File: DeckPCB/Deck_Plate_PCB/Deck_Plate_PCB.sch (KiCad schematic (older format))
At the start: 69 parts, among them J1 Raspberry_Pi_2_3, J2 NASA_Telemetry_Interface, J3 NASA PWR_Interface, J4 Motor_Inhibit, J5 SunnyBuddy_Inhibit, J6 Batt_JST_Conn, J7 BurWire_Inhibit, P1 Digital, P10 CONN_01X01, P11 CONN_01X01, P12 CONN_01X01, P13 CONN_01X01, P2 Power, P3 Analog, P4 Analog, P5 PWM, P6 PWM, P7 Communication, P8 CONN_01X01, P9 CONN_01X01, Q1 Q_NPN_BCE, Q2 2N7000, Q3 2N7000, U1 Adafruit_INA219_Breakout, U10 LM20, U11 Big_Easy_Driver, U12 Pi_Cam, U13 LM20, U2 LM2576T-5, U3 D24V25F9, U4 SunnyBuddy_Breakout, U5 LM2576T-5, U6 SF_Logic_Level_Conv, U7 Lidar_RangeFinder, U8 ADXL377, U9 TTL_Camera

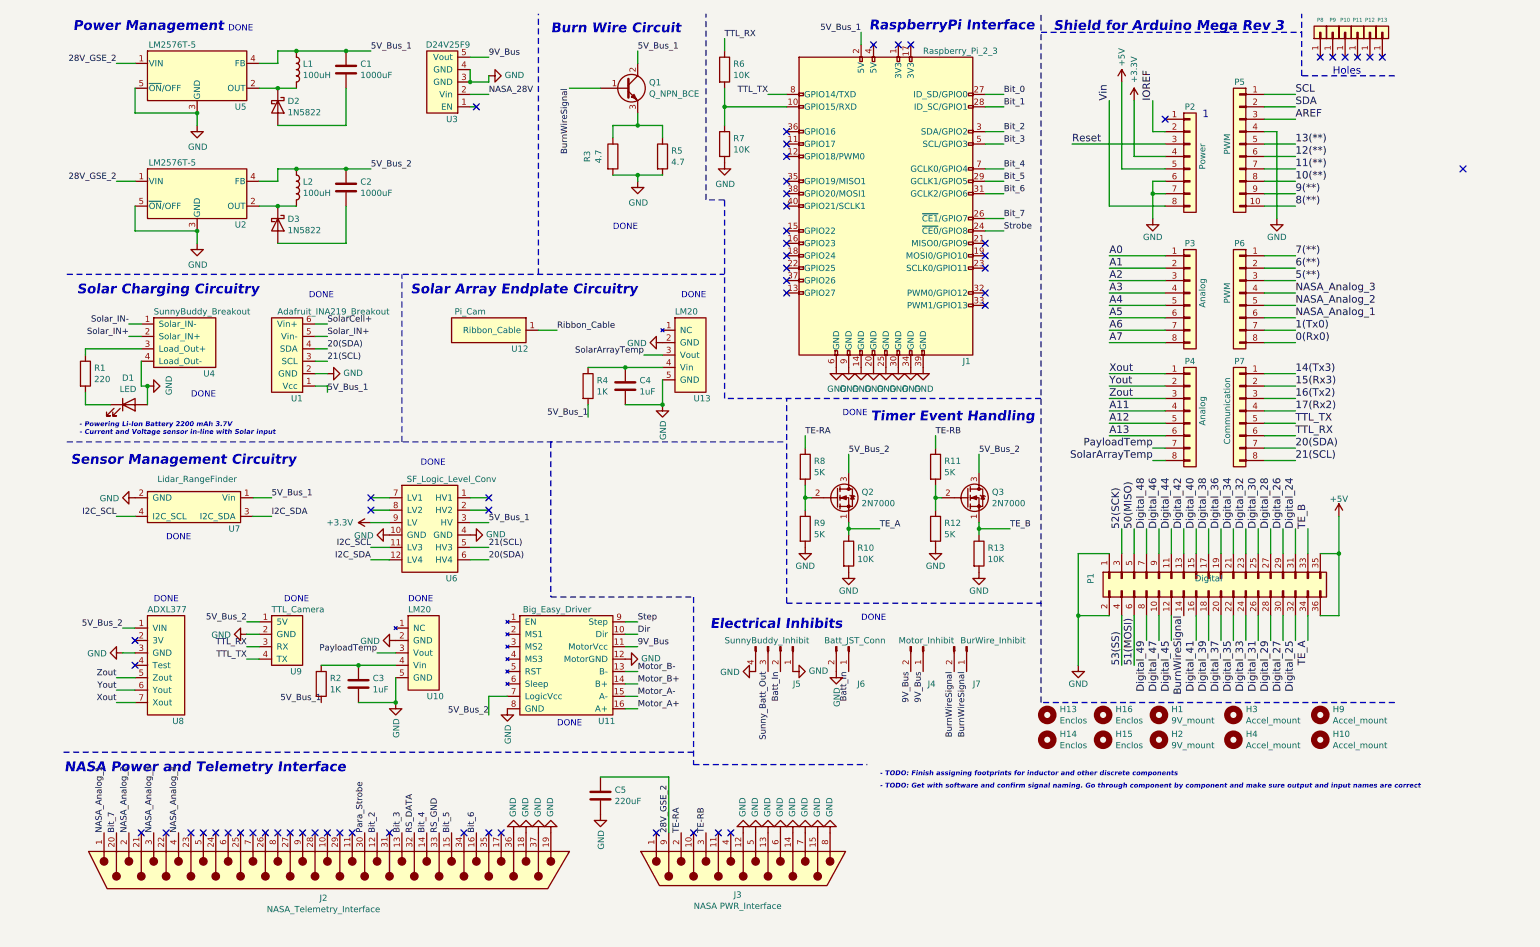
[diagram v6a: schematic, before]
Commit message: Created new daughter board for SunnyBuddy and RaspPi. Initial component layout complete.
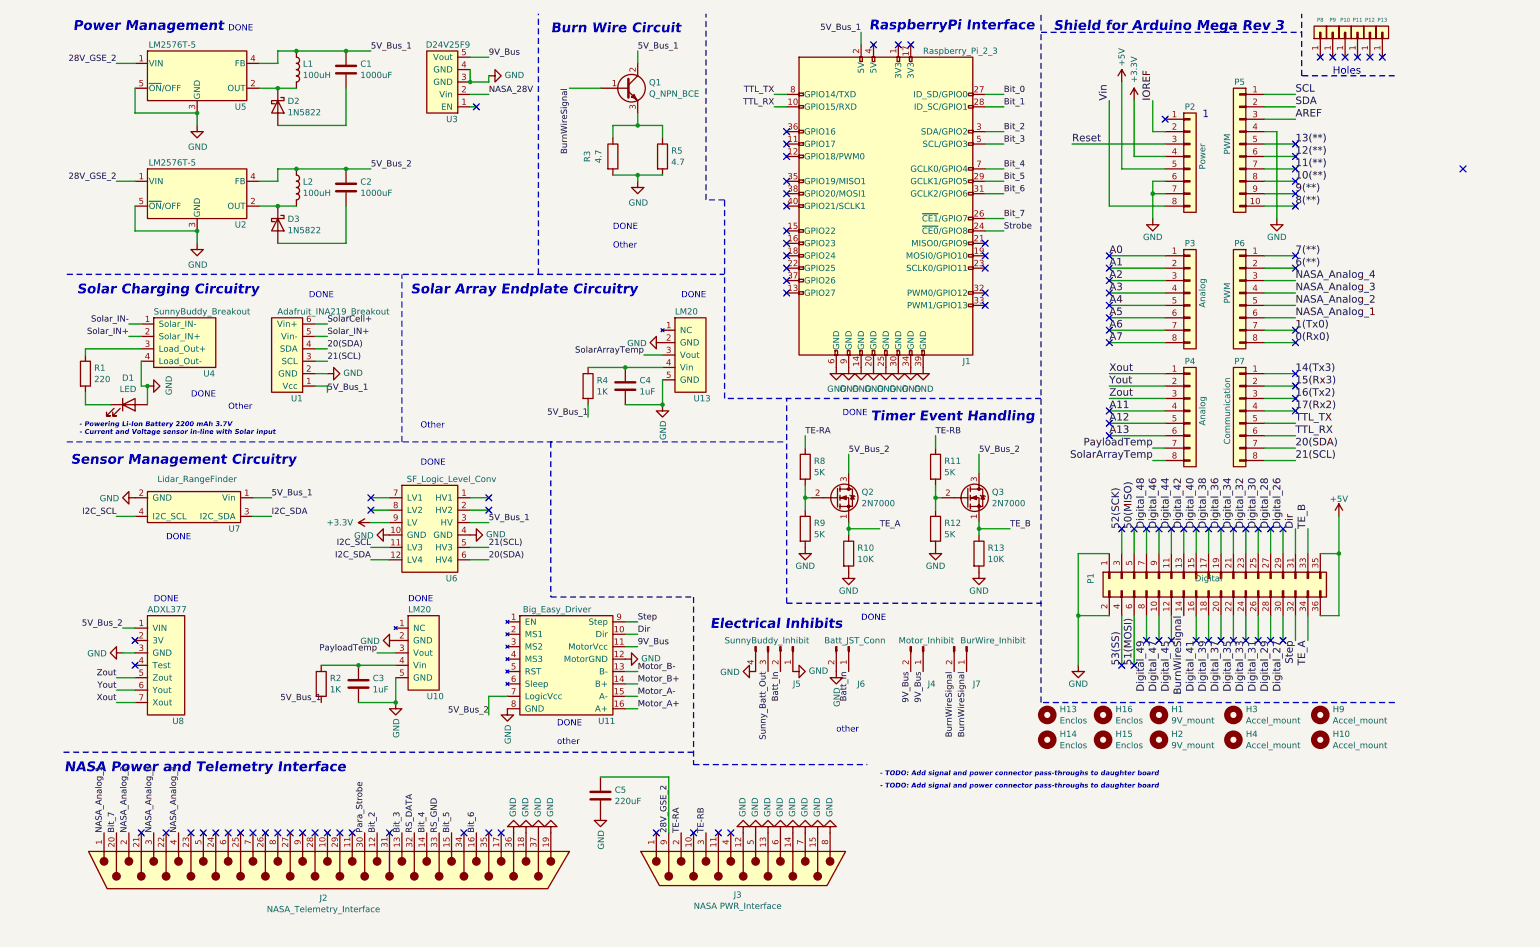
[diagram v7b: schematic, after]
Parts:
- removed R6, R7: 10K, Resistor_THT:R_Axial_DIN0207_L6.3mm_D2.5mm_P10.16mm_Horizontal, symbol Device:R
- removed U12: Pi_Cam, symbol Deck_Plate_PCB:Pi_Cam
- removed U9: TTL_Camera, Connector_PinHeader_2.54mm:PinHeader_1x04_P2.54mm_Vertical, symbol Deck_Plate_PCB:TTL_Camera
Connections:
- net 5(**) is gone; now on net NASA_Analog_4: P6.3 (Pin_3)
- net Digital_24 is gone; now on net Dir: P1.31 (Pin_31)
- net Digital_25 is gone; now on net Step: P1.32 (Pin_32)
- net TTL_RX: now also J1.10 (GPIO15/RXD)
- no-connect marks 59 -> 111
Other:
- note added: "- TODO: Add signal and power connector pass-throughs to daughter board\n"
- note added: "Other"
- note added: "Other\n"
- note added: "other"
- note added: "other\n"
- note removed: "- TODO: Finish assigning footprints for inductor and other discrete components\n"
- note removed: "- TODO: Get with software and confirm signal naming. Go through component by component and make sure output and input names are correct"
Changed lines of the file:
@@
 TE_B
 Text Label 10400 4650 1    60   ~ 0
-Digital_24
+Dir
 Text Label 10300 4650 1    60   ~ 0
 Digital_26
@@
 TE_A
 Text Label 10400 5550 3    60   ~ 0
-Digital_25
+Step
 Text Label 10300 5550 3    60   ~ 0
 Digital_27
@@
 6(**)
 Text Label 10400 2650 0    60   ~ 0
-5(**)
+NASA_Analog_4
 Text Label 10400 2750 0    60   ~ 0
 NASA_Analog_3
@@
 $EndComp
 $Comp
-L power:GND #PWR0114
-U 1 1 5E59C862
-P 5800 1700
-F 0 "#PWR0114" H 5800 1450 50  0001 C CNN
-F 1 "GND" H 5805 1527 50  0000 C CNN
-F 2 "" H 5800 1700 50  0001 C CNN
-F 3 "" H 5800 1700 50  0001 C CNN
-	1    5800 1700
-	1    0    0    -1
-$EndComp
-Text Label 5800 700  0    50   ~ 0
-TTL_RX
-Wire Wire Line
-	5800 800  5800 700
-$Comp
-L Device:R R6
-U 1 1 5E590153
-P 5800 950
-F 0 "R6" H 5870 996 50  0000 L CNN
-F 1 "10K" H 5870 905 50  0000 L CNN
-F 2 "Resistor_THT:R_Axial_DIN0207_L6.3mm_D2.5mm_P10.16mm_Horizontal" V 5730 950 50  0001 C CNN
-F 3 "~" H 5800 950 50  0001 C CNN
-	1    5800 950
-	1    0    0    -1
-$EndComp
-$Comp
-L Device:R R7
-U 1 1 5E58F78F
-P 5800 1550
-F 0 "R7" H 5870 1596 50  0000 L CNN
-F 1 "10K" H 5870 1505 50  0000 L CNN
-F 2 "Resistor_THT:R_Axial_DIN0207_L6.3mm_D2.5mm_P10.16mm_Horizontal" V 5730 1550 50  0001 C CNN
-F 3 "~" H 5800 1550 50  0001 C CNN
-	1    5800 1550
-	1    0    0    -1
-$EndComp
-Wire Wire Line
-	5800 1250 5800 1400
-Connection ~ 5800 1250
-Wire Wire Line
-	5800 1100 5800 1250
-Wire Wire Line
-	6300 1250 5800 1250
-Text Label 6150 1150 2    50   ~ 0
-TTL_TX
-Wire Wire Line
-	6300 1150 6150 1150
-$Comp
 L power:GND #PWR0115
 U 1 1 5E56BFDB
@@
 Wire Notes Line
 	500  2600 5800 2600
-$Comp
-L Deck_Plate_PCB:TTL_Camera U9
-U 1 1 5E7B135A
-P 1600 5900
-F 0 "U9" H 2300 6000 50  0000 L CNN
-F 1 "TTL_Camera" H 2150 6500 50  0000 L CNN
-F 2 "Connector_PinHeader_2.54mm:PinHeader_1x04_P2.54mm_Vertical" H 1600 5900 50  0001 C CNN
-F 3 "https://learn.adafruit.com/ttl-serial-camera" H 1600 5900 50  0001 C CNN
-	1    1600 5900
-	1    0    0    -1
-$EndComp
-Wire Wire Line
-	2050 5400 1950 5400
-Wire Wire Line
-	2050 5500 1950 5500
-Wire Wire Line
-	2050 5600 1950 5600
-Wire Wire Line
-	2050 5700 1950 5700
-Text Label 1950 5400 2    50   ~ 0
-5V_Bus_2
-$Comp
-L power:GND #PWR0124
-U 1 1 5E80010A
-P 1950 5500
-F 0 "#PWR0124" H 1950 5250 50  0001 C CNN
-F 1 "GND" V 1955 5372 50  0000 R CNN
-F 2 "" H 1950 5500 50  0001 C CNN
-F 3 "" H 1950 5500 50  0001 C CNN
-	1    1950 5500
-	0    1    1    0
-$EndComp
-Text Label 1950 5600 2    50   ~ 0
-TTL_RX
-Text Label 1950 5700 2    50   ~ 0
-TTL_TX
 $Comp
 L Deck_Plate_PCB:LM20 U10
@@
 	0    1    1    0
 $EndComp
-$Comp
-L Deck_Plate_PCB:Pi_Cam U12
-U 1 1 5E9ED3E3
-P 3500 3450
-F 0 "U12" H 4150 3700 50  0000 C CNN
-F 1 "Pi_Cam" H 3750 4000 50  0000 C CNN
-F 2 "" H 3500 3450 50  0001 C CNN
-F 3 "" H 3500 3450 50  0001 C CNN
-	1    3500 3450
-	1    0    0    -1
-$EndComp
-Wire Wire Line
-	4300 3050 4450 3050
-Text Label 4450 3050 0    50   ~ 0
-Ribbon_Cable
 Text Notes 2050 2900 2    79   Italic 16
 Solar Charging Circuitry\n\n
-Text Notes 5100 2900 2    79   Italic 16
-Solar Array Endplate Circuitry\n\n
 Wire Notes Line
 	500  3950 6300 3950
@@
 $EndComp
 Text Notes 7050 6650 0    39   Italic 8
-- TODO: Finish assigning footprints for inductor and other discrete components\n
-Text Notes 7050 6750 0    39   Italic 8
-- TODO: Get with software and confirm signal naming. Go through component by component and make sure output and input names are correct
+- TODO: Add signal and power connector pass-throughs to daughter board\n
 $Comp
 L Connector:Conn_01x02_Male J4
@@
 DONE
 Text Notes 2450 2800 0    50   ~ 0
-DONE
-Text Notes 2250 5250 0    50   ~ 0
 DONE
 Text Notes 1200 5250 0    50   ~ 0
@@
 Text Label 2600 3100 0    50   ~ 0
 Solar_IN+
+Text Notes 3350 3850 0    50   ~ 0
+Other\n
+Text Notes 4450 6400 0    50   ~ 0
+other
+Text Notes 6700 6300 0    50   ~ 0
+other\n
+Text Notes 1800 3700 0    50   ~ 0
+Other\n
+Text Notes 4900 2400 0    50   ~ 0
+Other
+NoConn ~ 9200 4650
+NoConn ~ 9300 4650
+NoConn ~ 9400 4650
+NoConn ~ 9500 4650
+NoConn ~ 9600 4650
+NoConn ~ 9700 4650
+NoConn ~ 9800 4650
+NoConn ~ 9900 4650
+NoConn ~ 10000 4650
+NoConn ~ 10100 4650
+NoConn ~ 10200 4650
+NoConn ~ 10300 4650
+NoConn ~ 10300 5550
+NoConn ~ 10200 5550
+NoConn ~ 10100 5550
+NoConn ~ 10000 5550
+NoConn ~ 9900 5550
+NoConn ~ 9800 5550
+NoConn ~ 9700 5550
+NoConn ~ 9600 5550
+NoConn ~ 9400 5550
+NoConn ~ 9300 5550
+NoConn ~ 9200 5550
+NoConn ~ 9100 5750
+NoConn ~ 9000 5750
+NoConn ~ 9100 4650
+NoConn ~ 9000 4650
+NoConn ~ 8900 3700
+NoConn ~ 8900 3800
+NoConn ~ 8900 3900
+NoConn ~ 8900 3150
+NoConn ~ 8900 3050
+NoConn ~ 8900 2950
+NoConn ~ 8900 2850
+NoConn ~ 8900 2750
+NoConn ~ 8900 2650
+NoConn ~ 8900 2550
+NoConn ~ 8900 2450
+NoConn ~ 10400 2450
+NoConn ~ 10400 2550
+NoConn ~ 10400 3050
+NoConn ~ 10400 3150
+NoConn ~ 10400 1550
+NoConn ~ 10400 1650
+NoConn ~ 10400 1750
+NoConn ~ 10400 1850
+NoConn ~ 10400 1950
+NoConn ~ 10400 2050
+NoConn ~ 10400 3400
+NoConn ~ 10400 3500
+NoConn ~ 10400 3600
+NoConn ~ 10400 3700
+Wire Wire Line
+	6300 1150 6200 1150
+Wire Wire Line
+	6300 1250 6200 1250
+Text Label 6200 1150 2    50   ~ 0
+TTL_TX
+Text Label 6200 1250 2    50   ~ 0
+TTL_RX
+Text Notes 5100 2900 2    79   Italic 16
+Solar Array Endplate Circuitry\n\n
+Text Notes 7050 6750 0    39   Italic 8
+- TODO: Add signal and power connector pass-throughs to daughter board\n
 $EndSCHEMATC

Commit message: Started routing of Deck_Plate_PCB, the main board.
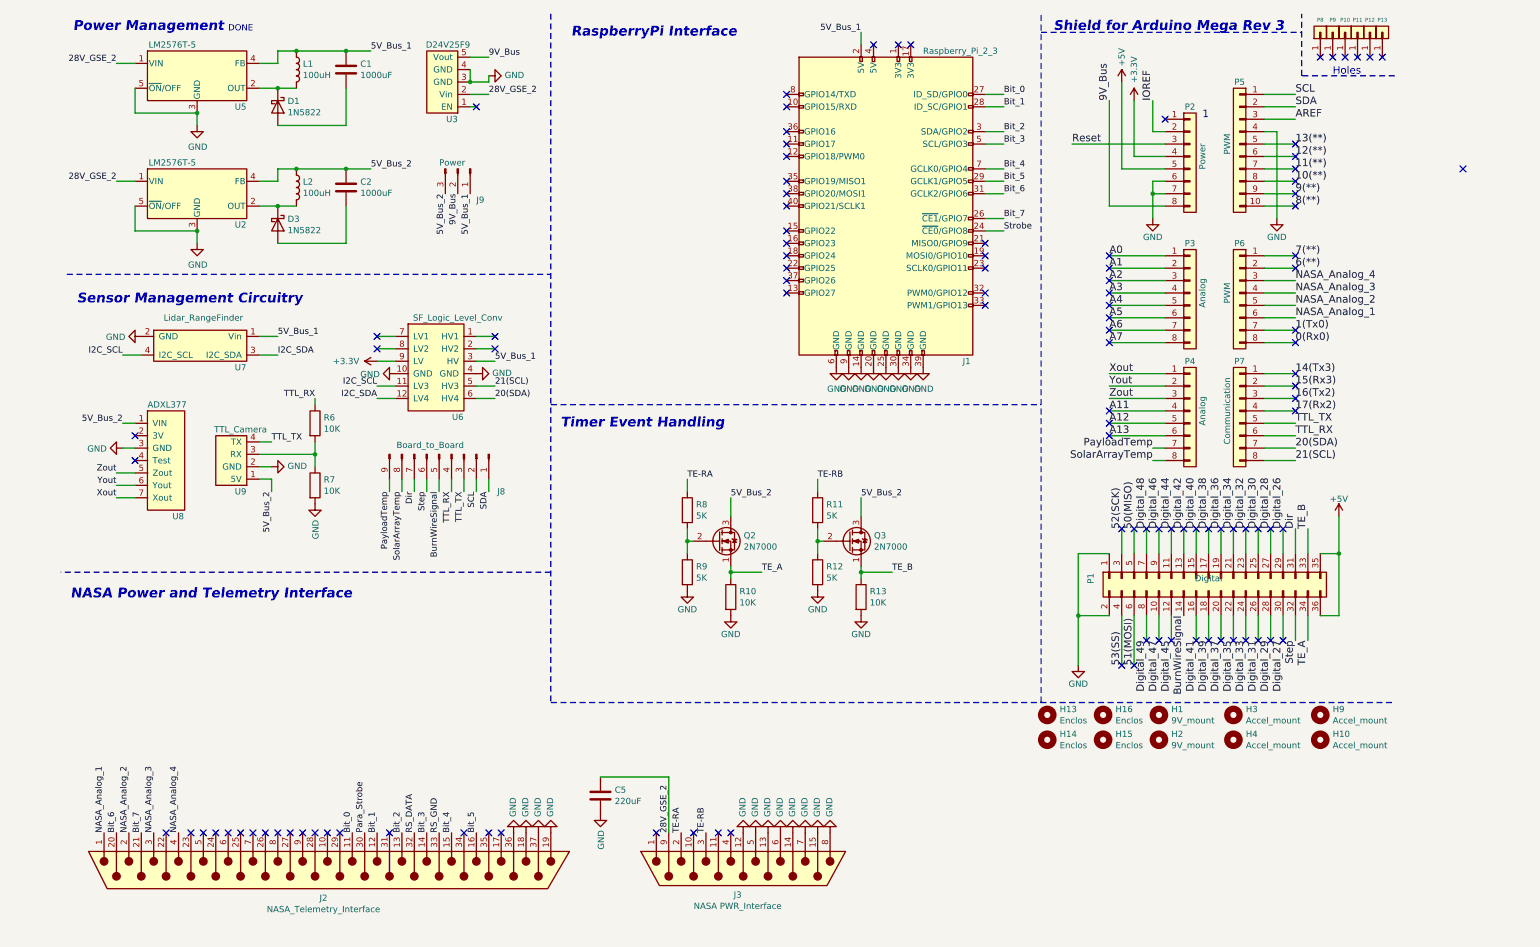
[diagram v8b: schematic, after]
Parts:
- removed C3, C4: 1uF, Capacitor_SMD:C_1206_3216Metric_Pad1.42x1.75mm_HandSolder, symbol Device:C
- removed D1: LED, LED_THT:LED_D3.0mm_Clear, symbol Device:LED
- removed D2: 1N5822, Diode_THT:D_DO-201AD_P15.24mm_Horizontal, symbol Diode:1N5822
- removed J4: Motor_Inhibit, Connector_PinHeader_2.54mm:PinHeader_1x02_P2.54mm_Vertical, symbol Connector:Conn_01x02_Male
- removed J5: SunnyBuddy_Inhibit, Connector_PinHeader_2.54mm:PinHeader_1x04_P2.54mm_Vertical, symbol Connector:Conn_01x04_Male
- removed J6: Batt_JST_Conn, Connector_JST:JST_PH_B2B-PH-K_1x02_P2.00mm_Vertical, symbol Connector:Conn_01x02_Male
- removed J7: BurWire_Inhibit, Connector_PinHeader_2.54mm:PinHeader_1x02_P2.54mm_Vertical, symbol Connector:Conn_01x02_Male
- removed Q1: Q_NPN_BCE, Package_TO_SOT_THT:TO-251-3_Vertical, symbol Device:Q_NPN_BCE
- removed R1: 220, Resistor_THT:R_Axial_DIN0207_L6.3mm_D2.5mm_P10.16mm_Horizontal, symbol Device:R
- removed R2, R4: 1K, Resistor_THT:R_Axial_DIN0207_L6.3mm_D2.5mm_P10.16mm_Horizontal, symbol Device:R
- removed R3, R5: 4.7, Resistor_THT:R_Axial_DIN0207_L6.3mm_D2.5mm_P10.16mm_Horizontal, symbol Device:R
- removed U1: Adafruit_INA219_Breakout, Deck_Plate_PCB:Adafruit_INA219_Breakout_header, symbol INA219_Breakout:Adafruit_INA219_Breakout
- removed U10, U13: LM20, Deck_Plate_PCB:LM20, symbol Deck_Plate_PCB:LM20
- removed U11: Big_Easy_Driver, Deck_Plate_PCB:Big_Easy_Driver, symbol Deck_Plate_PCB:Big_Easy_Driver
- removed U4: SunnyBuddy_Breakout, Deck_Plate_PCB:SunnyBuddy_Breakout, symbol Deck_Plate_PCB:SunnyBuddy_Breakout
- added D1: 1N5822, Diode_THT:D_DO-201AD_P12.70mm_Horizontal, symbol Diode:1N5822
- added J8: Board_to_Board, Connector_PinHeader_2.54mm:PinHeader_1x09_P2.54mm_Vertical, symbol Connector:Conn_01x09_Male
- added J9: Power, Connector_PinHeader_2.54mm:PinHeader_1x03_P2.54mm_Vertical, symbol Connector:Conn_01x03_Male
- added R6, R7: 10K, Resistor_THT:R_Axial_DIN0207_L6.3mm_D2.5mm_P10.16mm_Horizontal, symbol Device:R
- added U9: TTL_Camera, Connector_PinHeader_2.54mm:PinHeader_1x04_P2.54mm_Vertical, symbol Deck_Plate_PCB:TTL_Camera
- D3: footprint Diode_THT:D_DO-201AD_P15.24mm_Horizontal -> Diode_THT:D_DO-201AD_P12.70mm_Horizontal
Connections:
- net NASA_28V is gone; now on net 28V_GSE_2: U3.2 (Vin)
- net Vin is gone; now on net 9V_Bus: P2.8 (Pin_8)
- net 5V_Bus_1: now also J9.1 (Pin_1)
- net 5V_Bus_2: now also J9.3 (Pin_3), U9.1 (5V)
- net 9V_Bus: now also J9.2 (Pin_2)
- net Bit_0: now also J2.11
- net Bit_1: now also J2.12
- net Bit_2: now also J2.13; no longer J2.12
- net Bit_3: now also J2.14; no longer J2.13
- net Bit_4: now also J2.15; no longer J2.14
- net Bit_5: now also J2.16; no longer J2.15
- net Bit_6: now also J2.20; no longer J2.16
- net Bit_7: now also J2.21; no longer J2.20
- net BurnWireSignal: now also J8.5 (Pin_5)
- net Dir: now also J8.7 (Pin_7)
- net GND: now also R7.2, U9.2 (GND)
- net PayloadTemp: now also J8.9 (Pin_9)
- net SCL: now also J8.2 (Pin_2)
- net SDA: now also J8.1 (Pin_1)
- net SolarArrayTemp: now also J8.8 (Pin_8)
- net Step: now also J8.6 (Pin_6)
- net TTL_RX: now also J8.4 (Pin_4), R6.1; no longer J1.10 (GPIO15/RXD)
- net TTL_TX: now also J8.3 (Pin_3), U9.4 (TX); no longer J1.8 (GPIO14/TXD)
- net at L1.2, U5.2 (OUT): now also D1.1 (K)
- net at C1.2: now also D1.2 (A)
- new net: R6.2, R7.1, U9.3 (RX)
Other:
- note removed: "- Powering Li-Ion Battery 2200 mAh 3.7V\n- Current and Voltage sensor in-line with Solar input"
- note removed: "- TODO: Add signal and power connector pass-throughs to daughter board\n"
- note removed: "Burn Wire Circuit\n\n\n\n"
- note removed: "Electrical Inhibits\n\n\n\n"
- note removed: "Other"
- note removed: "Other\n"
- note removed: "Solar Array Endplate Circuitry\n\n"
- note removed: "Solar Charging Circuitry\n\n"
- note removed: "other"
- note removed: "other\n"
- moved on the sheet: Q2, Q3, R10, R11, R12, R13, R8, R9, U6, U7, U8
